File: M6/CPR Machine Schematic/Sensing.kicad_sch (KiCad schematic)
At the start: 14 parts, among them J12 Force Sensor, J9 I2C Port, U4 MCP6004, U5 MCP3021A0T-E_OT

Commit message: Condensed Header Pins
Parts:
- renumbered C6 to C7, C7 to C8, C8 to C9, J9 to J6, J12 to J9
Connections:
- net +3V3 renamed +3.3V
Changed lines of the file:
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@@
 		(dnp no)
 		(fields_autoplaced yes)
-		(property "Reference" "J9"
+		(property "Reference" "J6"
 			(at 53.34 93.9799 0)
 			(effects
@@
 			(project ""
 				(path "/8991fc77-975f-4978-a089-6b2a5e33f59b/2e704a40-db78-4cf7-9f7e-cfc586f5aeb3"
-					(reference "J9")
+					(reference "J6")
 					(unit 1)
 				)
@@
 		(on_board yes)
 		(dnp no)
-		(property "Reference" "J12"
+		(property "Reference" "J9"
 			(at 36.195 68.58 0)
 			(effects
@@
 			(project ""
 				(path "/8991fc77-975f-4978-a089-6b2a5e33f59b/2e704a40-db78-4cf7-9f7e-cfc586f5aeb3"
-					(reference "J12")
+					(reference "J9")
 					(unit 1)
 				)
@@
 		(dnp no)
 		(fields_autoplaced yes)
-		(property "Reference" "C6"
+		(property "Reference" "C7"
 			(at 53.34 59.69 90)
 			(effects
@@
 			(project ""
 				(path "/8991fc77-975f-4978-a089-6b2a5e33f59b/2e704a40-db78-4cf7-9f7e-cfc586f5aeb3"
-					(reference "C6")
+					(reference "C7")
 					(unit 1)
 				)
@@
 		(on_board yes)
 		(dnp no)
-		(property "Reference" "C8"
+		(property "Reference" "C9"
 			(at 116.332 39.624 0)
 			(effects
@@
 			(project "CPR Machine Schematic"
 				(path "/8991fc77-975f-4978-a089-6b2a5e33f59b/2e704a40-db78-4cf7-9f7e-cfc586f5aeb3"
-					(reference "C8")
+					(reference "C9")
 					(unit 1)
 				)
@@
 			)
 		)
-		(property "Value" "+3V3"
-			(at 113.03 22.8599 0)
-			(effects
-				(font
-					(size 1.27 1.27)
-				)
-				(justify left)
+		(property "Value" "+3.3V"
+			(at 110.49 19.05 0)
+			(effects
+				(font
+					(size 1.27 1.27)
+				)
 			)
 		)
@@
 			)
 		)
-		(property "Value" "+3V3"
+		(property "Value" "+3.3V"
 			(at 49.022 24.13 0)
 			(effects
@@
 		(on_board yes)
 		(dnp no)
-		(property "Reference" "C7"
+		(property "Reference" "C8"
 			(at 127.762 39.624 0)
 			(effects
@@
 			(project "CPR Machine Schematic"
 				(path "/8991fc77-975f-4978-a089-6b2a5e33f59b/2e704a40-db78-4cf7-9f7e-cfc586f5aeb3"
-					(reference "C7")
-					(unit 1)
-				)
+					(reference "C8")
+					(unit 1)
+				)

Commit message: Part Inventory
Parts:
- C7, J9, R13: Notes (none) -> Have: 5; now in the parts list
- R18: Notes (none) -> Have: 10+; now in the parts list
- TP5, TP6, TP7: now left out of the parts list
- U4, U5: Notes Have: 1 -> Have: 3

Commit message: GND testpoint, Main 0V diode redesign, Geograph Redesignate
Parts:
- renumbered C9 to C8, C8 to C9, R18 to R14, TP5 to TP6, TP6 to TP7, TP7 to TP8
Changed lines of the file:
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@@
 		(on_board yes)
 		(dnp no)
-		(property "Reference" "C9"
+		(property "Reference" "C8"
 			(at 116.332 39.624 0)
 			(effects
@@
 			(project "CPR Machine Schematic"
 				(path "/8991fc77-975f-4978-a089-6b2a5e33f59b/2e704a40-db78-4cf7-9f7e-cfc586f5aeb3"
-					(reference "C9")
+					(reference "C8")
 					(unit 1)
 				)
@@
 		(on_board yes)
 		(dnp no)
-		(property "Reference" "TP5"
+		(property "Reference" "TP6"
 			(at 67.564 29.972 0)
 			(effects
@@
 			(project "CPR Machine Schematic"
 				(path "/8991fc77-975f-4978-a089-6b2a5e33f59b/2e704a40-db78-4cf7-9f7e-cfc586f5aeb3"
-					(reference "TP5")
+					(reference "TP6")
 					(unit 1)
 				)
@@
 		(dnp no)
 		(fields_autoplaced yes)
-		(property "Reference" "R18"
+		(property "Reference" "R14"
 			(at 53.34 50.8 90)
 			(effects
@@
 			(project ""
 				(path "/8991fc77-975f-4978-a089-6b2a5e33f59b/2e704a40-db78-4cf7-9f7e-cfc586f5aeb3"
-					(reference "R18")
+					(reference "R14")
 					(unit 1)
 				)
@@
 		(dnp no)
 		(fields_autoplaced yes)
-		(property "Reference" "TP7"
+		(property "Reference" "TP8"
 			(at 35.56 97.0279 0)
 			(effects
@@
 			(project "CPR Machine Schematic"
 				(path "/8991fc77-975f-4978-a089-6b2a5e33f59b/2e704a40-db78-4cf7-9f7e-cfc586f5aeb3"
-					(reference "TP7")
+					(reference "TP8")
 					(unit 1)
 				)
@@
 		(dnp no)
 		(fields_autoplaced yes)
-		(property "Reference" "TP6"
+		(property "Reference" "TP7"
 			(at 35.56 90.9319 0)
 			(effects
@@
 			(project ""
 				(path "/8991fc77-975f-4978-a089-6b2a5e33f59b/2e704a40-db78-4cf7-9f7e-cfc586f5aeb3"
-					(reference "TP6")
+					(reference "TP7")
 					(unit 1)
 				)
@@
 		(on_board yes)
 		(dnp no)
-		(property "Reference" "C8"
+		(property "Reference" "C9"
 			(at 127.762 39.624 0)
 			(effects
@@
 			(project "CPR Machine Schematic"
 				(path "/8991fc77-975f-4978-a089-6b2a5e33f59b/2e704a40-db78-4cf7-9f7e-cfc586f5aeb3"
-					(reference "C8")
+					(reference "C9")
 					(unit 1)
 				)

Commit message: Swap out out-of-stock parts
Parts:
- U5: value MCP3021A0T-E_OT -> MCP3021A5T-E_OT; footprint 2679:IC_MCP3021A0T-E_OT -> 2679:IC_MCP3021A5T-E_OT; DigiKey_Part_Number MCP3021A0T-E/OTCT-ND -> MCP3021A5T-E/OTCT-ND
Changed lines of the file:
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@@
 			)
 		)
-		(property "Value" "MCP3021A0T-E_OT"
+		(property "Value" "MCP3021A5T-E_OT"
 			(at 82.55 25.4 0)
 			(effects
@@
 			)
 		)
-		(property "Footprint" "2679:IC_MCP3021A0T-E_OT"
+		(property "Footprint" "2679:IC_MCP3021A5T-E_OT"
 			(at 82.55 35.56 0)
 			(effects
@@
 			)
 		)
-		(property "Datasheet" "https://ww1.microchip.com/downloads/aemDocuments/documents/APID/ProductDocuments/DataSheets/20001805C.pdf"
+		(property "Datasheet" "https://www.digikey.com/en/products/detail/microchip-technology/MCP3021A5T-E-OT/593685"
 			(at 82.55 35.56 0)
 			(effects
@@
 			)
 		)
-		(property "DigiKey_Part_Number" "MCP3021A0T-E/OTCT-ND"
+		(property "DigiKey_Part_Number" "MCP3021A5T-E/OTCT-ND"
 			(at 82.55 35.56 0)
 			(effects

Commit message: More Revisions
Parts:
- J6: footprint Connector_PinHeader_2.54mm:PinHeader_1x02_P2.54mm_Vertical -> Connector_PinHeader_2.54mm:PinHeader_1x04_P2.54mm_Vertical; symbol Connector:Conn_01x02_Pin -> Connector:Conn_01x04_Pin; now in the parts list
- U5: footprint 2679:IC_MCP3021A5T-E_OT -> 2679:IC_MCP3021A0T-E_OT
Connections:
- net +3.3V: now also J6.1 (Pin_1)
- net GND: now also J6.2 (Pin_2)
- net I2C_SCL: now also J6.4 (Pin_4); no longer J6.2 (Pin_2)
- net I2C_SDA: now also J6.3 (Pin_3); no longer J6.1 (Pin_1)
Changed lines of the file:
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@@
 	(rectangle
 		(start 14.605 84.455)
-		(end 62.23 106.045)
+		(end 76.2 106.045)
 		(stroke
 			(width 0)
@@
 	(wire
 		(pts
+			(xy 55.88 91.44) (xy 57.15 91.44)
+		)
+		(stroke
+			(width 0)
+			(type default)
+		)
+	)
+	(wire
+		(pts
 			(xy 33.02 101.6) (xy 31.75 101.6)
 		)
@@
 	(wire
 		(pts
-			(xy 45.72 93.98) (xy 46.99 93.98)
+			(xy 45.72 96.52) (xy 57.15 96.52)
+		)
+		(stroke
+			(width 0)
+			(type default)
+		)
+	)
+	(wire
+		(pts
+			(xy 49.53 91.44) (xy 49.53 93.98)
 		)
 		(stroke
@@
 	(wire
 		(pts
-			(xy 45.72 88.9) (xy 45.72 93.98)
+			(xy 45.72 88.9) (xy 45.72 96.52)
 		)
 		(stroke
@@
 	(wire
 		(pts
-			(xy 45.72 96.52) (xy 45.72 101.6)
+			(xy 45.72 99.06) (xy 45.72 101.6)
 		)
 		(stroke
@@
 	(wire
 		(pts
-			(xy 45.72 96.52) (xy 46.99 96.52)
+			(xy 45.72 99.06) (xy 57.15 99.06)
 		)
 		(stroke
@@
 		(pts
 			(xy 43.18 77.47) (xy 43.18 76.2)
+		)
+		(stroke
+			(width 0)
+			(type default)
+		)
+	)
+	(wire
+		(pts
+			(xy 49.53 93.98) (xy 57.15 93.98)
 		)
 		(stroke
@@
 	)
 	(symbol
-		(lib_id "Connector:Conn_01x02_Pin")
-		(at 52.07 93.98 0)
+		(lib_id "Connector:Conn_01x04_Pin")
+		(at 62.23 93.98 0)
 		(mirror y)
 		(unit 1)
 		(exclude_from_sim no)
-		(in_bom no)
+		(in_bom yes)
 		(on_board yes)
 		(dnp no)
 		(fields_autoplaced yes)
 		(property "Reference" "J6"
-			(at 53.34 93.9799 0)
+			(at 63.5 93.9799 0)
 			(effects
 				(font
@@
 		)
 		(property "Value" "I2C Port"
-			(at 53.34 96.5199 0)
+			(at 63.5 96.5199 0)
 			(effects
 				(font
@@
 			)
 		)
-		(property "Footprint" "Connector_PinHeader_2.54mm:PinHeader_1x02_P2.54mm_Vertical"
-			(at 52.07 93.98 0)
+		(property "Footprint" "Connector_PinHeader_2.54mm:PinHeader_1x04_P2.54mm_Vertical"
+			(at 62.23 93.98 0)
 			(effects
 				(font
@@
 		)
 		(property "Datasheet" "~"
-			(at 52.07 93.98 0)
-			(effects
-				(font
-					(size 1.27 1.27)
-				)
-				(hide yes)
-			)
-		)
-		(property "Description" "Generic connector, single row, 01x02, script generated"
-			(at 52.07 93.98 0)
+			(at 62.23 93.98 0)
+			(effects
+				(font
+					(size 1.27 1.27)
+				)
+				(hide yes)
+			)
+		)
+		(property "Description" "Generic connector, single row, 01x04, script generated"
+			(at 62.23 93.98 0)
 			(effects
 				(font
@@
 		)
 		(property "Notes" ""
-			(at 52.07 93.98 0)
+			(at 62.23 93.98 0)
 			(effects
 				(font
@@
 		)
 		(property "MPN" ""
-			(at 52.07 93.98 0)
+			(at 62.23 93.98 0)
 			(effects
 				(font
@@
 		)
 		(property "OC_FARNELL" ""
-			(at 52.07 93.98 0)
+			(at 62.23 93.98 0)
 			(effects
 				(font
@@
 		)
 		(property "OC_NEWARK" ""
-			(at 52.07 93.98 0)
+			(at 62.23 93.98 0)
 			(effects
 				(font
@@
 		)
 		(property "PACKAGE" ""
-			(at 52.07 93.98 0)
+			(at 62.23 93.98 0)
 			(effects
 				(font
@@
 		)
 		(property "SUPPLIER" ""
-			(at 52.07 93.98 0)
+			(at 62.23 93.98 0)
 			(effects
 				(font
@@
 		)
 		(pin "1"
+		)
+		(pin "3"
+		)
+		(pin "4"
 		)
 		(instances
@@
 			)
 		)
-		(property "Footprint" "2679:IC_MCP3021A5T-E_OT"
+		(property "Footprint" "2679:IC_MCP3021A0T-E_OT"
 			(at 82.55 35.56 0)
 			(effects
@@
 	)
 	(symbol
+		(lib_id "power:GND")
+		(at 49.53 91.44 180)
+		(unit 1)
+		(exclude_from_sim no)
+		(in_bom yes)
+		(on_board yes)
+		(dnp no)
+		(fields_autoplaced yes)
+		(property "Reference" "#PWR033"
+			(at 49.53 85.09 0)
+			(effects
+				(font
+					(size 1.27 1.27)
+				)
+				(hide yes)
+			)
+		)
+		(property "Value" "GND"
+			(at 49.53 86.36 0)
+			(effects
+				(font
+					(size 1.27 1.27)
+				)
+			)
+		)
+		(property "Footprint" ""
+			(at 49.53 91.44 0)
+			(effects
+				(font
+					(size 1.27 1.27)
+				)
+				(hide yes)
+			)
+		)
+		(property "Datasheet" ""
+			(at 49.53 91.44 0)
+			(effects
+				(font
+					(size 1.27 1.27)
+				)
+				(hide yes)
+			)
+		)
+		(property "Description" "Power symbol creates a global label with name \"GND\" , ground"
+			(at 49.53 91.44 0)
+			(effects
+				(font
+					(size 1.27 1.27)
+				)
+				(hide yes)
+			)
+		)
+		(pin "1"
+		)
+		(instances
+			(project ""
+				(path "/8991fc77-975f-4978-a089-6b2a5e33f59b/2e704a40-db78-4cf7-9f7e-cfc586f5aeb3"
+					(reference "#PWR033")
+					(unit 1)
+				)
+			)
+		)
+	)
+	(symbol
 		(lib_id "Device:C")
 		(at 110.49 41.91 180)
@@
 					(unit 1)
 				)
+			)
+		)
+	)
+	(symbol
+		(lib_id "power:+3.3V")
+		(at 55.88 91.44 0)
+		(unit 1)
+		(exclude_from_sim no)
+		(in_bom yes)
+		(on_board yes)
+		(dnp no)
+		(fields_autoplaced yes)
+		(property "Reference" "#PWR032"
+			(at 55.88 95.25 0)
+			(effects
+				(font
+					(size 1.27 1.27)
+				)
+				(hide yes)
+			)
+		)
+		(property "Value" "+3.3V"
+			(at 55.88 86.36 0)
+			(effects
+				(font
+					(size 1.27 1.27)
+				)
+			)
+		)
+		(property "Footprint" ""
+			(at 55.88 91.44 0)
+			(effects
+				(font
+					(size 1.27 1.27)
+				)
+				(hide yes)
+			)
+		)
+		(property "Datasheet" ""
+			(at 55.88 91.44 0)
+			(effects
+				(font
+					(size 1.27 1.27)
+				)
+				(hide yes)
+			)
+		)
+		(property "Description" "Power symbol creates a global label with name \"+3.3V\""
+			(at 55.88 91.44 0)
+			(effects
+				(font
+					(size 1.27 1.27)
+				)
+				(hide yes)
+			)
+		)
+		(pin "1"
+		)
+		(instances
+			(project ""
+				(path "/8991fc77-975f-4978-a089-6b2a5e33f59b/2e704a40-db78-4cf7-9f7e-cfc586f5aeb3"
+					(reference "#PWR032")
+					(unit 1)
+				)

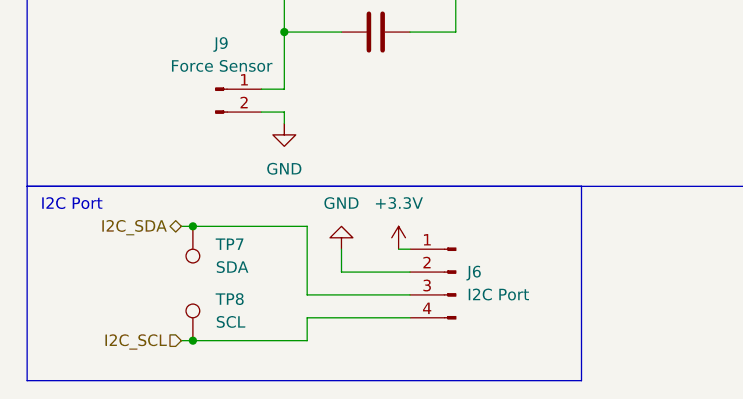
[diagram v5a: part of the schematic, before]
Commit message: Reduced Xt30 interference w/ raspi IO
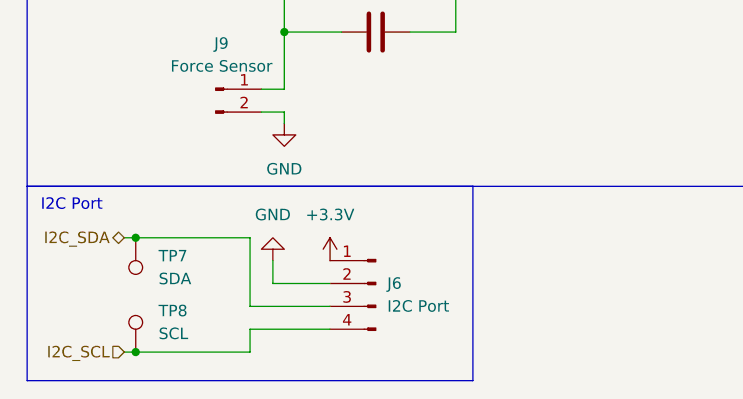
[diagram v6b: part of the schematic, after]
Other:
- moved on the sheet: J6, TP7, TP8
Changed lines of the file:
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@@
 	(rectangle
 		(start 14.605 84.455)
-		(end 76.2 106.045)
+		(end 64.135 106.045)
 		(stroke
 			(width 0)
@@
 	)
 	(junction
-		(at 33.02 88.9)
+		(at 26.67 90.17)
 		(diameter 0)
 		(color 0 0 0 0)
@@
 	)
 	(junction
-		(at 33.02 101.6)
+		(at 26.67 102.87)
 		(diameter 0)
 		(color 0 0 0 0)
@@
 	(wire
 		(pts
-			(xy 55.88 91.44) (xy 57.15 91.44)
-		)
-		(stroke
-			(width 0)
-			(type default)
-		)
-	)
-	(wire
-		(pts
-			(xy 33.02 101.6) (xy 31.75 101.6)
-		)
-		(stroke
-			(width 0)
-			(type default)
-		)
-	)
-	(wire
-		(pts
-			(xy 45.72 101.6) (xy 33.02 101.6)
+			(xy 26.67 102.87) (xy 25.4 102.87)
+		)
+		(stroke
+			(width 0)
+			(type default)
+		)
+	)
+	(wire
+		(pts
+			(xy 39.37 102.87) (xy 26.67 102.87)
 		)
 		(stroke
@@
 	(wire
 		(pts
-			(xy 45.72 96.52) (xy 57.15 96.52)
-		)
-		(stroke
-			(width 0)
-			(type default)
-		)
-	)
-	(wire
-		(pts
-			(xy 49.53 91.44) (xy 49.53 93.98)
+			(xy 39.37 97.79) (xy 48.26 97.79)
+		)
+		(stroke
+			(width 0)
+			(type default)
+		)
+	)
+	(wire
+		(pts
+			(xy 41.91 92.71) (xy 41.91 95.25)
 		)
 		(stroke
@@
 	(wire
 		(pts
-			(xy 45.72 88.9) (xy 45.72 96.52)
+			(xy 39.37 90.17) (xy 39.37 97.79)
 		)
 		(stroke
@@
 	(wire
 		(pts
-			(xy 33.02 88.9) (xy 45.72 88.9)
+			(xy 26.67 90.17) (xy 39.37 90.17)
 		)
 		(stroke
@@
 	(wire
 		(pts
-			(xy 31.75 88.9) (xy 33.02 88.9)
+			(xy 25.4 90.17) (xy 26.67 90.17)
 		)
 		(stroke
@@
 	(wire
 		(pts
-			(xy 45.72 99.06) (xy 45.72 101.6)
+			(xy 39.37 100.33) (xy 39.37 102.87)
 		)
 		(stroke
@@
 	(wire
 		(pts
-			(xy 45.72 99.06) (xy 57.15 99.06)
+			(xy 39.37 100.33) (xy 48.26 100.33)
 		)
 		(stroke
@@
 	(wire
 		(pts
-			(xy 49.53 93.98) (xy 57.15 93.98)
+			(xy 41.91 95.25) (xy 48.26 95.25)
 		)
 		(stroke
@@
 	(hierarchical_label "I2C_SCL"
 		(shape input)
-		(at 31.75 101.6 180)
+		(at 25.4 102.87 180)
 		(effects
 			(font
@@
 	(hierarchical_label "I2C_SDA"
 		(shape bidirectional)
-		(at 31.75 88.9 180)
+		(at 25.4 90.17 180)
 		(effects
 			(font
@@
 	(symbol
 		(lib_id "Connector:Conn_01x04_Pin")
-		(at 62.23 93.98 0)
+		(at 53.34 95.25 0)
 		(mirror y)
 		(unit 1)
@@
 		(fields_autoplaced yes)
 		(property "Reference" "J6"
-			(at 63.5 93.9799 0)
+			(at 54.61 95.2499 0)
 			(effects
 				(font
@@
 		)
 		(property "Value" "I2C Port"
-			(at 63.5 96.5199 0)
+			(at 54.61 97.7899 0)
 			(effects
 				(font
@@
 		)
 		(property "Footprint" "Connector_PinHeader_2.54mm:PinHeader_1x04_P2.54mm_Vertical"
-			(at 62.23 93.98 0)
+			(at 53.34 95.25 0)
 			(effects
 				(font
@@
 		)
 		(property "Datasheet" "~"
-			(at 62.23 93.98 0)
+			(at 53.34 95.25 0)
 			(effects
 				(font
@@
 		)
 		(property "Description" "Generic connector, single row, 01x04, script generated"
-			(at 62.23 93.98 0)
+			(at 53.34 95.25 0)
 			(effects
 				(font
@@
 		)
 		(property "Notes" ""
-			(at 62.23 93.98 0)
+			(at 53.34 95.25 0)
 			(effects
 				(font
@@
 		)
 		(property "MPN" ""
-			(at 62.23 93.98 0)
+			(at 53.34 95.25 0)
 			(effects
 				(font
@@
 		)
 		(property "OC_FARNELL" ""
-			(at 62.23 93.98 0)
+			(at 53.34 95.25 0)
 			(effects
 				(font
@@
 		)
 		(property "OC_NEWARK" ""
-			(at 62.23 93.98 0)
+			(at 53.34 95.25 0)
 			(effects
 				(font
@@
 		)
 		(property "PACKAGE" ""
-			(at 62.23 93.98 0)
+			(at 53.34 95.25 0)
 			(effects
 				(font
@@
 		)
 		(property "SUPPLIER" ""
-			(at 62.23 93.98 0)
+			(at 53.34 95.25 0)
 			(effects
 				(font
@@
 	(symbol
 		(lib_id "power:GND")
-		(at 49.53 91.44 180)
+		(at 41.91 92.71 180)
 		(unit 1)
 		(exclude_from_sim no)
@@
 		(fields_autoplaced yes)
 		(property "Reference" "#PWR033"
-			(at 49.53 85.09 0)
+			(at 41.91 86.36 0)
 			(effects
 				(font
@@
 		)
 		(property "Value" "GND"
-			(at 49.53 86.36 0)
+			(at 41.91 87.63 0)
 			(effects
 				(font
@@
 		)
 		(property "Footprint" ""
-			(at 49.53 91.44 0)
+			(at 41.91 92.71 0)
 			(effects
 				(font
@@
 		)
 		(property "Datasheet" ""
-			(at 49.53 91.44 0)
+			(at 41.91 92.71 0)
 			(effects
 				(font
@@
 		)
 		(property "Description" "Power symbol creates a global label with name \"GND\" , ground"
-			(at 49.53 91.44 0)
+			(at 41.91 92.71 0)
 			(effects
 				(font
@@
 	(symbol
 		(lib_id "Connector:TestPoint")
-		(at 33.02 101.6 0)
+		(at 26.67 102.87 0)
 		(unit 1)
 		(exclude_from_sim no)
@@
 		(fields_autoplaced yes)
 		(property "Reference" "TP8"
-			(at 35.56 97.0279 0)
+			(at 29.21 98.2979 0)
 			(effects
 				(font
@@
 		)
 		(property "Value" "SCL"
-			(at 35.56 99.5679 0)
+			(at 29.21 100.8379 0)
 			(effects
 				(font
@@
 		)
 		(property "Footprint" "TestPoint:TestPoint_Pad_D1.5mm"
-			(at 38.1 101.6 0)
+			(at 31.75 102.87 0)
 			(effects
 				(font
@@
 		)
 		(property "Datasheet" "~"
-			(at 38.1 101.6 0)
+			(at 31.75 102.87 0)
 			(effects
 				(font
@@
 		)
 		(property "Description" "test point"
-			(at 33.02 101.6 0)
+			(at 26.67 102.87 0)
 			(effects
 				(font
@@
 		)
 		(property "MPN" ""
-			(at 33.02 101.6 0)
+			(at 26.67 102.87 0)
 			(effects
 				(font
@@
 		)
 		(property "OC_FARNELL" ""
-			(at 33.02 101.6 0)
+			(at 26.67 102.87 0)
 			(effects
 				(font
@@
 		)
 		(property "OC_NEWARK" ""
-			(at 33.02 101.6 0)
+			(at 26.67 102.87 0)
 			(effects
 				(font
@@
 		)
 		(property "PACKAGE" ""
-			(at 33.02 101.6 0)
+			(at 26.67 102.87 0)
 			(effects
 				(font
@@
 		)
 		(property "SUPPLIER" ""
-			(at 33.02 101.6 0)
+			(at 26.67 102.87 0)
 			(effects
 				(font
@@
 	(symbol
 		(lib_id "Connector:TestPoint")
-		(at 33.02 88.9 180)
+		(at 26.67 90.17 180)
 		(unit 1)
 		(exclude_from_sim no)
@@
 		(fields_autoplaced yes)
 		(property "Reference" "TP7"
-			(at 35.56 90.9319 0)
+			(at 29.21 92.2019 0)
 			(effects
 				(font
@@
 		)
 		(property "Value" "SDA"
-			(at 35.56 93.4719 0)
+			(at 29.21 94.7419 0)
 			(effects
 				(font
@@
 		)
 		(property "Footprint" "TestPoint:TestPoint_Pad_D1.5mm"
-			(at 27.94 88.9 0)
+			(at 21.59 90.17 0)
 			(effects
 				(font
@@
 		)
 		(property "Datasheet" "~"
-			(at 27.94 88.9 0)
+			(at 21.59 90.17 0)
 			(effects
 				(font
@@
 		)
 		(property "Description" "test point"
-			(at 33.02 88.9 0)
+			(at 26.67 90.17 0)
 			(effects
 				(font
@@
 		)
 		(property "MPN" ""
-			(at 33.02 88.9 0)
+			(at 26.67 90.17 0)
 			(effects
 				(font
@@
 		)
 		(property "OC_FARNELL" ""
-			(at 33.02 88.9 0)
+			(at 26.67 90.17 0)
 			(effects
 				(font
@@
 		)
 		(property "OC_NEWARK" ""
-			(at 33.02 88.9 0)
+			(at 26.67 90.17 0)
 			(effects
 				(font
@@
 		)
 		(property "PACKAGE" ""
-			(at 33.02 88.9 0)
+			(at 26.67 90.17 0)
 			(effects
 				(font
@@
 		)
 		(property "SUPPLIER" ""
-			(at 33.02 88.9 0)
+			(at 26.67 90.17 0)
 			(effects
 				(font
@@
 	(symbol
 		(lib_id "power:+3.3V")
-		(at 55.88 91.44 0)
+		(at 48.26 92.71 0)
 		(unit 1)
 		(exclude_from_sim no)
@@
 		(fields_autoplaced yes)
 		(property "Reference" "#PWR032"
-			(at 55.88 95.25 0)
+			(at 48.26 96.52 0)
 			(effects
 				(font
@@
 		)
 		(property "Value" "+3.3V"
-			(at 55.88 86.36 0)
+			(at 48.26 87.63 0)
 			(effects
 				(font
@@
 		)
 		(property "Footprint" ""
-			(at 55.88 91.44 0)
+			(at 48.26 92.71 0)
 			(effects
 				(font
@@
 		)
 		(property "Datasheet" ""
-			(at 55.88 91.44 0)
+			(at 48.26 92.71 0)
 			(effects
 				(font
@@
 		)
 		(property "Description" "Power symbol creates a global label with name \"+3.3V\""
-			(at 55.88 91.44 0)
-			(effects
-				(font
+			(at 48.26 92.71 0)
+			(effects
+				(font
